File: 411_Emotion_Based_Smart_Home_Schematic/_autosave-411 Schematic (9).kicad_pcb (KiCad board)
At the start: 2 copper layers, 123 x 48 mm, 25 parts, among them Q1 NSS1C301ET4G, Q2 NSS1C301ET4G, Q3 NSS1C301ET4G, U4 HC-SR04

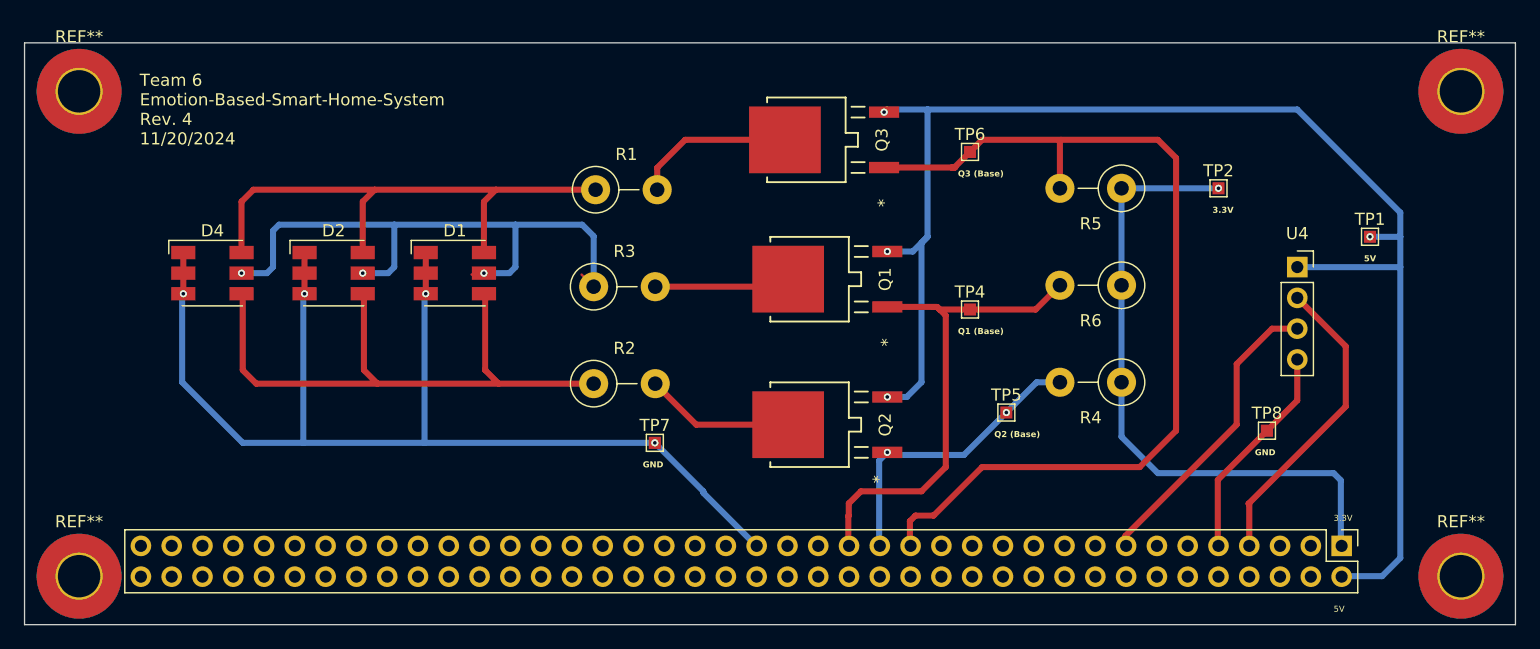
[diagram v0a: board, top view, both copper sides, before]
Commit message: Updated schematic.
Added limiting resistors to each GPIO pins.
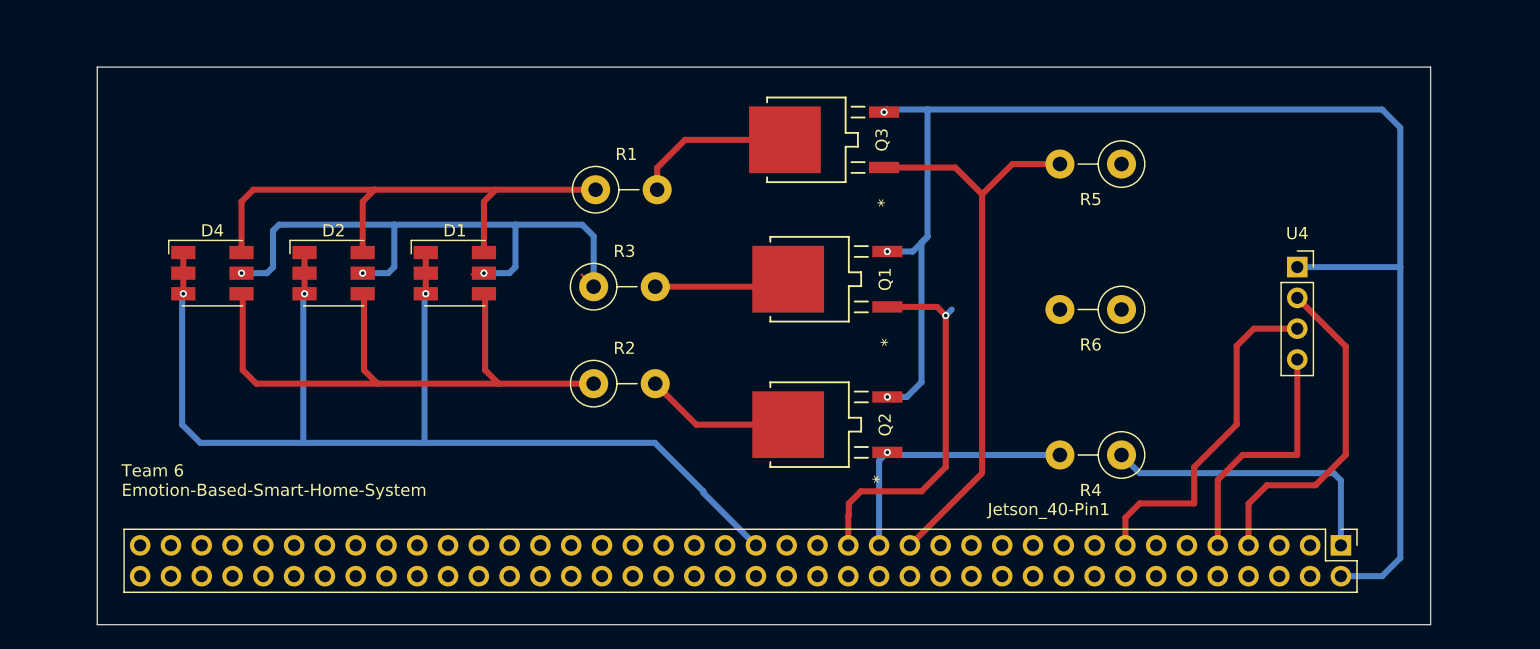
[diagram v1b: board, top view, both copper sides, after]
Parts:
- removed 40_Pin_Header1: ~, Connector_PinHeader_2.54mm:PinHeader_2x40_P2.54mm_Vertical
- removed REF** (x4): MountingHole_3.5mm_Pad_TopBottom, MountingHole:MountingHole_3.5mm_Pad_TopBottom
- removed TP1: 5V, TestPoint:TestPoint_Pad_1.0x1.0mm
- removed TP2: 3.3V, TestPoint:TestPoint_Pad_1.0x1.0mm
- removed TP4: Q1, TestPoint:TestPoint_Pad_1.0x1.0mm
- removed TP5: Q2, TestPoint:TestPoint_Pad_1.0x1.0mm
- removed TP6: Q3, TestPoint:TestPoint_Pad_1.0x1.0mm
- removed TP7, TP8: GND, TestPoint:TestPoint_Pad_1.0x1.0mm
- added Jetson_40-Pin1: ~, Connector_PinHeader_2.54mm:PinHeader_2x40_P2.54mm_Vertical, F.Cu at (148.1, 93.5)
- moved R4 6.00 mm to (130.0, 86.0)
- moved R5 2.00 mm to (130.0, 62.0)
- moved R6 2.00 mm to (130.0, 74.0)
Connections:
- net 5V renamed /5V
- U4 pad 2: /Trigger -> /Ultrasonic Trigger
- U4 pad 3: /Echo -> Net-(Jetson_40-Pin1-GPIO12)
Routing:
- net Net-(Jetson_40-Pin1-GPIO01): track 79.5 -> 47.9 mm
- net Net-(Jetson_40-Pin1-3.3V): track 53.5 -> 24.3 mm, vias 1 -> 0
- net Net-(Jetson_40-Pin1-GPIO12): track 0.00 -> 28.5 mm
- net /Ultrasonic Trigger: track 0.00 -> 27.7 mm
- net /Trigger: track 25.5 -> 0.00 mm
- net /Echo: track 25.0 -> 0.00 mm
- net Net-(Jetson_40-Pin1-GPIO13): track 41.4 -> 31.0 mm, vias 0 -> 1
- net Net-(U4-GND): track 18.1 -> 20.7 mm
- net Net-(Jetson_40-Pin1-GPIO11): track 25.1 -> 22.6 mm, vias 2 -> 1
- net GND: track 95.2 -> 97.3 mm, vias 4 -> 3
- net /5V: track 121.1 -> 122.7 mm, vias 4 -> 3
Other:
- board size 123 x 48 mm -> 110 x 46 mm
- board text added: "Team 6 Emotion-Based-Smart-Home-System"
- board text removed: "3.3V"
- board text removed: "5V"
- board text removed: "GND"
- board text removed: "Q1 (Base)"
- board text removed: "Q2 (Base)"
- board text removed: "Q3 (Base)"
- board text removed: "Team 6 Emotion-Based-Smart-Home-System Rev. 4 11/20/2024"
